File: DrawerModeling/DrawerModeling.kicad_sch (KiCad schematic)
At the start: 3 parts

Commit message: edit_1 scheme first success
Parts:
- removed BT1: 9V, Battery:BatteryHolder_Keystone_103_1x20mm, symbol Device:Battery
- removed D1: LED, LED_SMD:LED_1812_4532Metric, symbol Device:LED
- added C1, C2: C_Polarized, symbol Device:C_Polarized
- added D1, D2, D3, D4: D_45deg, symbol Device:D_45deg
- added R2: 51, symbol Device:R
- added TR1: TEZ1.5-D-2, Transformer_THT:Transformer_Breve_TEZ-28x33, symbol Transformer:TEZ1.5-D-2
- added U1: AD633JRZ-R7, AD633JRZ-R7:SOIC127P600X175-8N, symbol AD633JRZ-R7:AD633JRZ-R7
- added V1: VSIN, symbol Simulation_SPICE:VSIN
- R1: value 420 -> 51; footprint Resistor_SMD:R_1020_2550Metric_Pad1.33x5.20mm_HandSolder -> (none)
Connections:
- net at R1.1: now also R2.2, U1.1 (Y1), U1.7 (X1)
- net at R1.2: now also D2.2 (A), D3.1 (K), TR1.6
- new net: D1.2 (A), D4.1 (K), TR1.10
- new net: C2.1, D3.2 (A), D4.2 (A), U1.3 (-VS)
- new net: C1.2, C2.2, R2.1, TR1.7, TR1.9, U1.2 (Y2), U1.4 (Z), U1.8 (X2)
- new net: C1.1, D1.1 (K), D2.1 (K), U1.6 (+VS)
- new net: TR1.1, V1.1
- new net: TR1.5, V1.2

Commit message: edit_2 still developing scheme
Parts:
- added C3: C, symbol Device:C
- added R3, R4: 51, symbol Device:R
- added R5: 4.7k, symbol Device:R
- added RV1: R_Potentiometer, symbol Device:R_Potentiometer
- added U2: L7805, symbol Regulator_Linear:L7805
- added U3: LM393_Block, Package_DIP:DIP-8_W7.62mm, symbol Ki_Library:LM393_Block
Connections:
- net at C2.1, D3.2 (A), D4.2 (A)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: now also R4.2, U2.2 (GND), U3.4 (V-), U3.6 (-)
- net at C1.2, C2.2, R2.1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: now also U3.2 (-)
- net at U1.5 (W): now also U3.3 (+)
- net at C1.1, D1.1 (K), D2.1 (K)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: now also R3.1
- new net: R3.2, R4.1, U2.1 (IN)
- new net: C3.2, RV1.1
- new net: R5.2, U2.3 (OUT), U3.5 (+), U3.8 (V+)
- new net: R5.1, U3.1

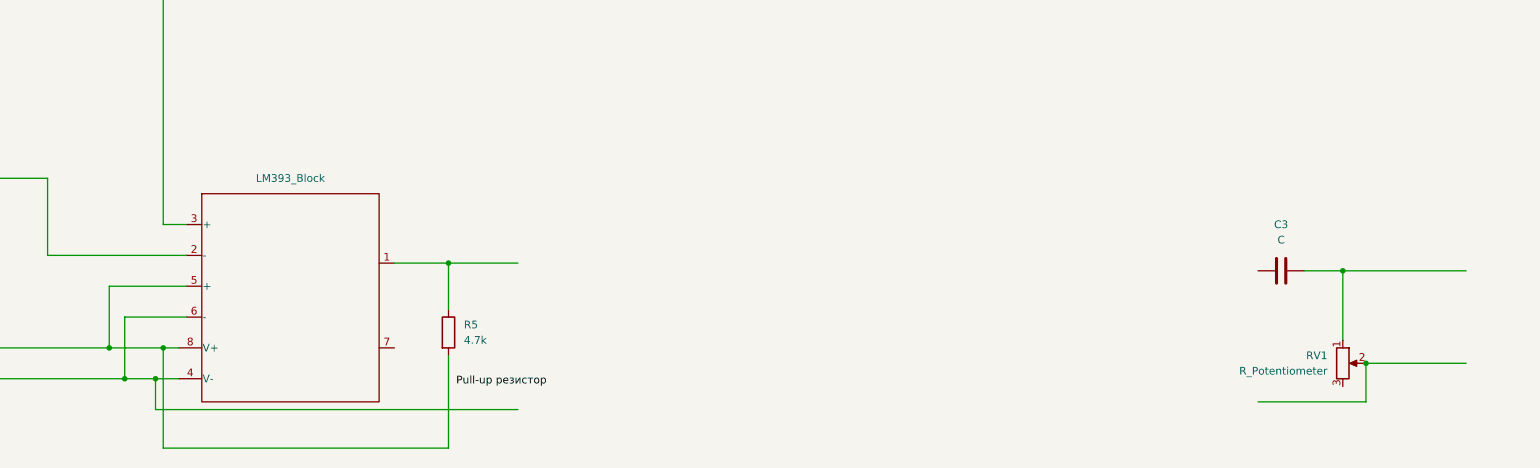
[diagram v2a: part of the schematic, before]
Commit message: edit_3 added tl082 block
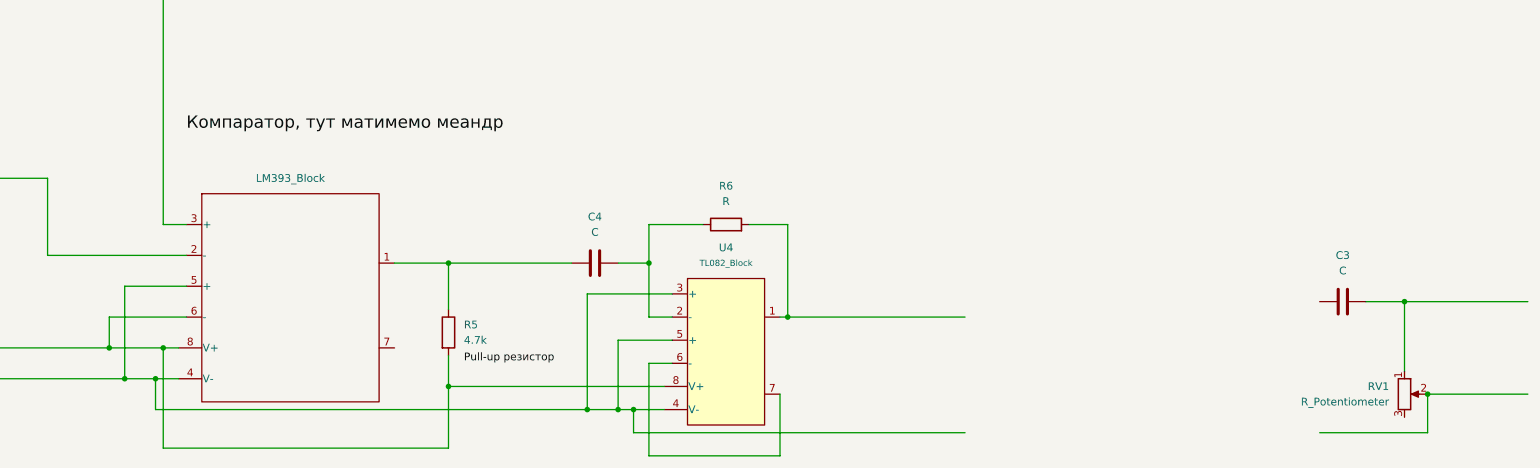
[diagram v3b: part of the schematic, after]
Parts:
- added C4: C, symbol Device:C
- added R6: R, symbol Device:R
- added U4: TL082_Block, Package_DIP:DIP-8_W7.62mm, symbol Ki_Library:TL082_Block
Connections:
- net at C2.1, D3.2 (A), D4.2 (A)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: now also U3.5 (+), U4.3 (+), U4.4 (V-), U4.5 (+); no longer U3.6 (-)
- net at R5.2, U2.3 (OUT), U3.8 (V+): now also U3.6 (-), U4.8 (V+); no longer U3.5 (+)
- net at R5.1, U3.1: now also C4.1
- new net: C4.2, R6.1, U4.2 (-)
- new net: R6.2, U4.1
- new net: U4.6 (-), U4.7
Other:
- moved on the sheet: C3, RV1

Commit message: edit_4 Scheme logic is completed
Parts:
- removed TR1: TEZ1.5-D-2, Transformer_THT:Transformer_Breve_TEZ-28x33, symbol Transformer:TEZ1.5-D-2
- added D5, D6: D, symbol Device:D
- added SW1: SW_NKK_GW12LJPCF, Button_Switch_THT:SW_NKK_GW12LJP, symbol Switch:SW_NKK_GW12LJPCF
- added TR1: TEZ4.0-D-2, Transformer_THT:Transformer_Breve_TEZ-35x42, symbol Transformer:TEZ4.0-D-2
- added U5: ~, Connector_PinHeader_2.54mm:PinHeader_1x20_P2.54mm_Vertical, symbol Ki_Library:BlackPill_Socket
- added U6: LM1117LD-3.3, Package_SON:WSON-8-1EP_4x4mm_P0.8mm_EP2.2x3mm, symbol Regulator_Linear:LM1117LD-3.3
- added U7: AD633JRZ-R7, AD633JRZ-R7:SOIC127P600X175-8N, symbol AD633JRZ-R7:AD633JRZ-R7
- added V3: VPWL, symbol Simulation_SPICE:VPWL
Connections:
- net at R3.2, R4.1, U2.1 (IN): now also U5.GND, U6.1 (GND), V3.2
- net GND: now reaches R4.2, U2.2 (GND), U3.4 (V-), U3.5 (+), U4.3 (+), U4.4 (V-), U4.5 (+)
- net GND: now also C1.2, C2.2, R2.1, RV1.2, U1.2 (Y2), U1.4 (Z), U1.8 (X2), U3.2 (-), TR1.7, TR1.9, U7.2 (Y2), U7.4 (Z), U7.8 (X2); no longer C2.1, D3.2 (A), D4.2 (A), U1.3 (-VS)
- net at C3.1: now also D5.1 (K), D6.2 (A)
- net at C3.2, RV1.1: now also U7.7 (X1)
- net at D1.2 (A), D4.1 (K): now also TR1.10
- net at R6.2, U4.1: now also SW1.2 (B), U5.B10
- net at C1.1, D1.1 (K), D2.1 (K)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: now also U6.2 (VI), U6.3 (VI), U6.4 (VI), U7.6 (+VS)
- net at D2.2 (A), D3.1 (K), R1.2: now also TR1.6
- net at V1.1: now also TR1.1
- net at V1.2: now also TR1.5
- new net: D6.1 (K), SW1.3 (C)
- new net: C2.1, D3.2 (A), D4.2 (A), U1.3 (-VS), U7.3 (-VS)
- new net: U5.3V3, U6.5 (VO), U6.6 (VO), U6.7 (VO), U6.9 (VO)
- new net: D5.2 (A), SW1.1 (A)
- new net: U5.B2, U7.1 (Y1), V3.1
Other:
- moved on the sheet: C1, C2, C3, C4, D1, D2, D3, D4, R1, R2, R3, R4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

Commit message: edit_5 Significant errors fixed
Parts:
- added SW2: SW_DIP_x01, symbol Switch:SW_DIP_x01
- added U10: TLP222A, Package_DIP:DIP-4_W7.62mm, symbol Relay_SolidState:TLP222A
- added U8: L7815, symbol Regulator_Linear:L7815
- added U9: L7915, symbol Regulator_Linear:L7915
- C1, C2: value C_Polarized -> 500uF
- R1, R2: value 51 -> 75k
- R3: value 51 -> 58.695k
- R4: value 51 -> 91.304k
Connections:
- net GND: now also U8.2 (GND), U9.1 (GND)
- net at D6.1 (K): no longer SW1.3 (C)
- net at C2.1, D3.2 (A), D4.2 (A): now also U9.2 (VI); no longer U1.3 (-VS), U7.3 (-VS)
- net at C1.1, D1.1 (K), D2.1 (K)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: now also U8.1 (IN); no longer U1.6 (+VS), U7.6 (+VS)
- net at D5.2 (A): no longer SW1.1 (A)
- net at R6.2, U4.1, U5.B10: no longer SW1.2 (B)
- new net: U1.3 (-VS), U7.3 (-VS), U9.3 (VO)
- new net: U1.6 (+VS), U7.6 (+VS), U8.3 (OUT)
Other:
- moved on the sheet: C2, SW1

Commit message: edit_5 All for today
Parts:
- removed SW2: SW_DIP_x01, symbol Switch:SW_DIP_x01
- added R7: R, symbol Device:R
- added SW3: SW_SPDT_321, symbol Switch:SW_SPDT_321
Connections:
- net GND: now also U10.1, SW3.1 (C)
- net at D6.1 (K): now also U10.4
- net at C3.2, RV1.1: now also SW3.3 (A); no longer U7.7 (X1)
- net at R6.2, U4.1, U5.B10: now also U10.3
- net at SW1.2 (B): now also R5.2, U2.3 (OUT), U3.6 (-), U3.8 (V+), U4.8 (V+)
- net at SW1.5 (A): now also R7.1
- new net: SW3.2 (B), U7.7 (X1)
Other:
- moved on the sheet: SW1, U10

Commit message: edit_6 counting [200~
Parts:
- removed U10: TLP222A, Package_DIP:DIP-4_W7.62mm, symbol Relay_SolidState:TLP222A
- added R8: 595, symbol Device:R
- added U11: TLP222A-2, Package_DIP:DIP-8_W7.62mm, symbol Relay_SolidState:TLP222A-2
- C3: value C -> 200u
- C4: value C -> 100u
- R5: value 4.7k -> 1k
- R6: value R -> 1000
- R7: value R -> 2975
- RV1: value R_Potentiometer -> 1000
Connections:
- net GND: now also R7.1, R8.1
- net at D6.1 (K): now also U11.8
- net at U1.3 (-VS), U7.3 (-VS), U9.3 (VO): now also SW1.2 (B)
- net at D5.2 (A): now also U11.6
- net at R6.2, U4.1, U5.B10: now also U11.5, U11.7
- net at SW1.1 (A): now also SW1.6 (KG), U11.4
- net at R5.2, U2.3 (OUT), U3.6 (-)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: no longer SW1.2 (B)
- net at SW1.3 (C): now also SW1.4 (KR), U11.2
- net at SW1.5 (A): now also R8.2; no longer R7.1
- net at R7.2: now also U11.1, U11.3
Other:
- moved on the sheet: D5, D6, R7, SW1

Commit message: edit_7 testing simulation(1)
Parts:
- C4: value 100u -> 5n
- R6: value 1000 -> 4928
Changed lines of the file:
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@@
+		)
+	)
+	(label "Їсть 5мА"
+		(at 168.91 110.49 0)
+		(effects
+			(font
+				(size 2.032 2.032)
+			)
+			(justify left bottom)
 		)
 	)
@@
 			)
 		)
-		(property "Value" "1000"
+		(property "Value" "4928"
 			(at 326.39 158.75 90)
 			(effects
@@
 			)
 		)
-		(property "Value" "100u"
+		(property "Value" "5n"
 			(at 304.8 163.83 90)
 			(effects
